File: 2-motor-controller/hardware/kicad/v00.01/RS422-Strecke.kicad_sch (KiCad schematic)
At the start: 3 parts, among them U401 MAX3488EEPA

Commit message: Motor-Controller: alle Blaetter nach den Zeichenregeln (Rahmen, Gruppen), 5-V-Zweig mit 2 x 4,7 uF, Titelfelder Version 00.01; Pruefung gegen Blockschaltbild 78/78
Co-Authored-By: Claude Opus 5.5 <noreply@anthropic.com>
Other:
- company: (none) -> SuAn-Autopilot-Projekt
- title: (none) -> Motor-Controller V2.0 – Datenstrecke RS422
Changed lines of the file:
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@@
 	(generator_version "10.0")
 	(paper "A4")
+	(title_block
+		(title "Motor-Controller V2.0 – Datenstrecke RS422")
+		(date "2026-10-09")
+		(rev "00.01")
+		(company "SuAn-Autopilot-Projekt")
+	)
 	(wire
 		(pts

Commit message: Motor-Controller: Loetbilder zugeordnet (eigene: Dialight 551, TL1105, KEMET C320, Display-Leiste), Platine 150 x 130 mm mit allen 94 Teilen angeordnet - Bauteilauswahl 00.23, Anforderungen 00.11, Stueckliste 00.19
Co-Authored-By: Claude Opus 5.5 <noreply@anthropic.com>
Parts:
- C401: footprint (none) -> Motor-Controller:C_KEMET_C320_L5.1mm_W4.1mm_P2.54mm
- R401: footprint (none) -> Resistor_THT:R_Axial_DIN0207_L6.3mm_D2.5mm_P10.16mm_Horizontal
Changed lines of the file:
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@@
 			)
 		)
-		(property "Footprint" ""
+		(property "Footprint" "Motor-Controller:C_KEMET_C320_L5.1mm_W4.1mm_P2.54mm"
 			(at 116.84 64.77 0)
 			(hide yes)
@@
 			)
 		)
-		(property "Footprint" ""
+		(property "Footprint" "Resistor_THT:R_Axial_DIN0207_L6.3mm_D2.5mm_P10.16mm_Horizontal"
 			(at 154.94 82.55 0)
 			(hide yes)

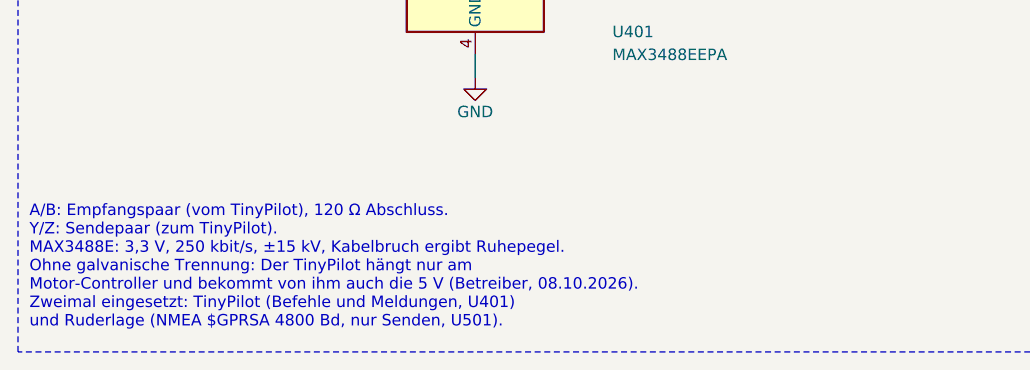
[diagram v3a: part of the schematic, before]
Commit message: 12 V zum Steuerstand statt 5 V: eigener Regler 12->5 V (3 A) am Steuerstand
Vom Motorraum gehen 12 V (rot/schwarz) zum Regler am Steuerstand, von dort 5 V
(zweites rot/schwarzes Paar) zur PyPilot-Einheit.
- Systembeschreibung, TODO (Frage 1 geloescht, Frage 18 gekuerzt)
- Motor-Controller: F13 (motorcontroller 00.13), Bauteilauswahl 00.26,
  Blockschaltbild 00.07, Stueckliste 00.21: J7.8 = +12 V hinter D2, ohne
  eigene Sicherung (Betreiber 13.10.2026); zweiter 5-V-Zweig entfernt
- KiCad v00.01: Blatt "5V PyPilot" und 8 Bauteile entfernt; ERC 0 Fehler,
  Paritaet 0, pruefung_blockschaltbild 00.03: 78/78
- Phase 1 Verdrahtungsplaene: Basic (Regler vor TinyPilot), Dual Display
  (Masse zum Regler); Vermerk Einbauort

Co-Authored-By: Claude Opus 5.5 <noreply@anthropic.com>
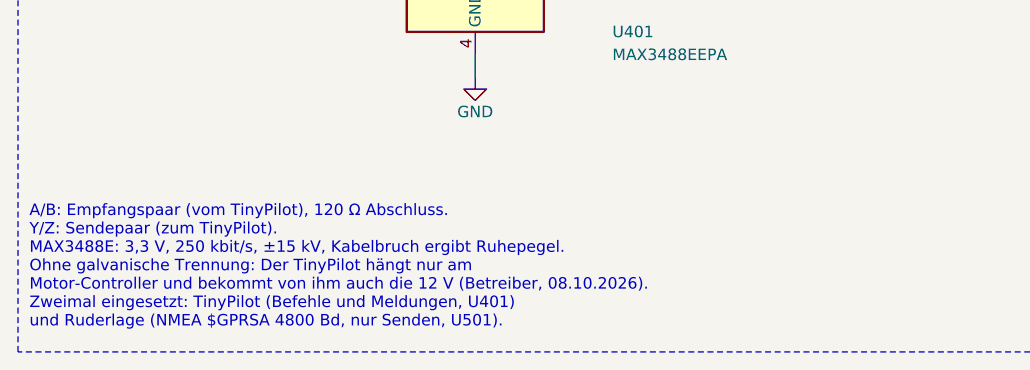
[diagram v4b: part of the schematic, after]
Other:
- note added: "A/B: Empfangspaar (vom TinyPilot), 120 Ω Abschluss. Y/Z: Sendepaar (zum TinyPilot). MAX3488E: 3,3 V, 250 kbit/s, ±15 kV, Kabelbruch ergibt Ruhepegel. Ohne galvanische Trennung: Der TinyPilot hängt nur am Motor-Controller und bekommt von ihm auch die 12 V (Betreiber, 08.10.2026). Zweimal eingesetzt: TinyPilot (Befehle und Meldungen, U401) und Ruderlage (NMEA $GPRSA 4800 Bd, nur Senden, U501)."
- note removed: "A/B: Empfangspaar (vom TinyPilot), 120 Ω Abschluss. Y/Z: Sendepaar (zum TinyPilot). MAX3488E: 3,3 V, 250 kbit/s, ±15 kV, Kabelbruch ergibt Ruhepegel. Ohne galvanische Trennung: Der TinyPilot hängt nur am Motor-Controller und bekommt von ihm auch die 5 V (Betreiber, 08.10.2026). Zweimal eingesetzt: TinyPilot (Befehle und Meldungen, U401) und Ruderlage (NMEA $GPRSA 4800 Bd, nur Senden, U501)."
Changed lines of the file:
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@@
 		)
 	)
-	(text "A/B: Empfangspaar (vom TinyPilot), 120 Ω Abschluss.\nY/Z: Sendepaar (zum TinyPilot).\nMAX3488E: 3,3 V, 250 kbit/s, ±15 kV, Kabelbruch ergibt Ruhepegel.\nOhne galvanische Trennung: Der TinyPilot hängt nur am\nMotor-Controller und bekommt von ihm auch die 5 V (Betreiber, 08.10.2026).\nZweimal eingesetzt: TinyPilot (Befehle und Meldungen, U401)\nund Ruderlage (NMEA $GPRSA 4800 Bd, nur Senden, U501)."
+	(text "A/B: Empfangspaar (vom TinyPilot), 120 Ω Abschluss.\nY/Z: Sendepaar (zum TinyPilot).\nMAX3488E: 3,3 V, 250 kbit/s, ±15 kV, Kabelbruch ergibt Ruhepegel.\nOhne galvanische Trennung: Der TinyPilot hängt nur am\nMotor-Controller und bekommt von ihm auch die 12 V (Betreiber, 08.10.2026).\nZweimal eingesetzt: TinyPilot (Befehle und Meldungen, U401)\nund Ruderlage (NMEA $GPRSA 4800 Bd, nur Senden, U501)."
 		(exclude_from_sim no)
 		(at 77.47 134.62 0)
@@
 		)
 	)
-	(sheet_instances
-		(path "/"
-			(page "1")
-		)
-	)
